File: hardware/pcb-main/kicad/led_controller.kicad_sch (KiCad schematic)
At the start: 5 parts, among them IC1 SN74AHCT125PWR

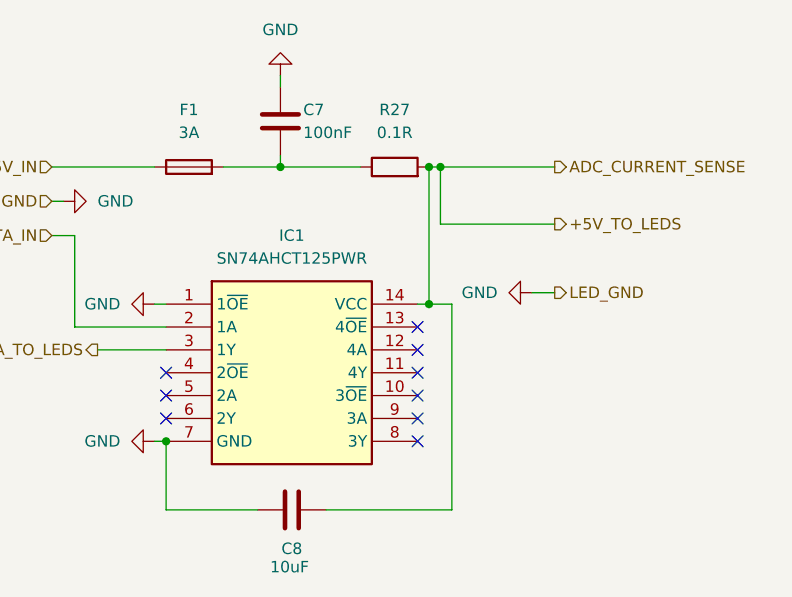
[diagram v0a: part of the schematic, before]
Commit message: Finished sensor redesign
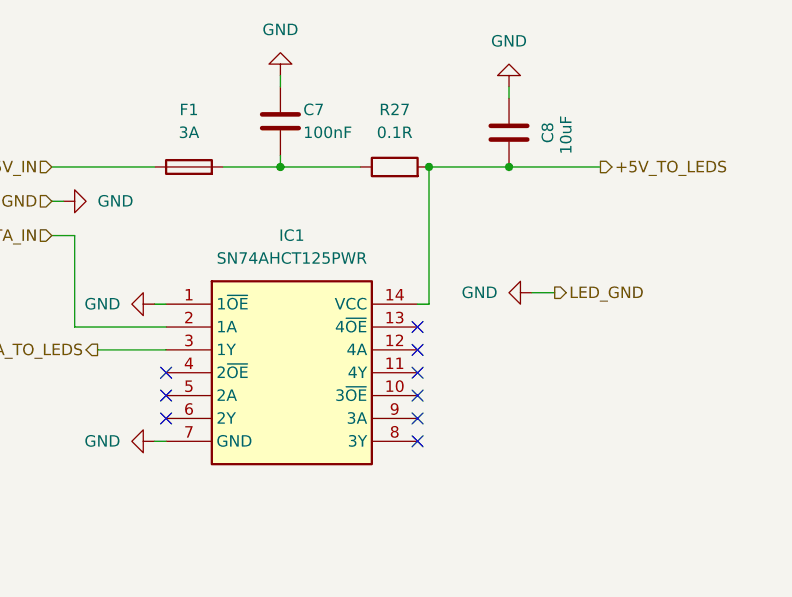
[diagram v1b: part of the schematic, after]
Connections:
- net +5V_TO_LEDS: now also C8.2; no longer C8.1
- net GND: now also C8.1; no longer C8.2
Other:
- moved on the sheet: C8
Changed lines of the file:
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@@
 	)
 	(junction
-		(at 146.05 88.9)
+		(at 184.15 58.42)
 		(diameter 0)
 		(color 0 0 0 0)
@@
 	)
 	(junction
-		(at 175.26 73.66)
-		(diameter 0)
-		(color 0 0 0 0)
-	)
-	(junction
-		(at 176.53 58.42)
-		(diameter 0)
-		(color 0 0 0 0)
-	)
-	(junction
 		(at 175.26 58.42)
 		(diameter 0)
@@
 	(wire
 		(pts
-			(xy 146.05 96.52) (xy 156.21 96.52)
-		)
-		(stroke
-			(width 0)
-			(type default)
-		)
-	)
-	(wire
-		(pts
-			(xy 176.53 64.77) (xy 176.53 58.42)
+			(xy 184.15 49.53) (xy 184.15 50.8)
 		)
 		(stroke
@@
 	(wire
 		(pts
-			(xy 176.53 58.42) (xy 189.23 58.42)
-		)
-		(stroke
-			(width 0)
-			(type default)
-		)
-	)
-	(wire
-		(pts
-			(xy 163.83 96.52) (xy 177.8 96.52)
-		)
-		(stroke
-			(width 0)
-			(type default)
-		)
-	)
-	(wire
-		(pts
 			(xy 144.78 88.9) (xy 146.05 88.9)
 		)
@@
 	(wire
 		(pts
-			(xy 177.8 73.66) (xy 175.26 73.66)
-		)
-		(stroke
-			(width 0)
-			(type default)
-		)
-	)
-	(wire
-		(pts
-			(xy 175.26 58.42) (xy 176.53 58.42)
+			(xy 184.15 58.42) (xy 194.31 58.42)
+		)
+		(stroke
+			(width 0)
+			(type default)
+		)
+	)
+	(wire
+		(pts
+			(xy 175.26 58.42) (xy 184.15 58.42)
 		)
 		(stroke
@@
 	(wire
 		(pts
-			(xy 189.23 64.77) (xy 176.53 64.77)
-		)
-		(stroke
-			(width 0)
-			(type default)
-		)
-	)
-	(wire
-		(pts
-			(xy 177.8 96.52) (xy 177.8 73.66)
-		)
-		(stroke
-			(width 0)
-			(type default)
-		)
-	)
-	(wire
-		(pts
 			(xy 152.4 58.42) (xy 158.75 58.42)
-		)
-		(stroke
-			(width 0)
-			(type default)
-		)
-	)
-	(wire
-		(pts
-			(xy 146.05 88.9) (xy 146.05 96.52)
 		)
 		(stroke
@@
 	(hierarchical_label "+5V_TO_LEDS"
 		(shape output)
-		(at 189.23 64.77 0)
-		(effects
-			(font
-				(size 1.27 1.27)
-			)
-			(justify left)
-		)
-	)
-	(hierarchical_label "ADC_CURRENT_SENSE"
-		(shape output)
-		(at 189.23 58.42 0)
+		(at 194.31 58.42 0)
 		(effects
 			(font
@@
 	(symbol
 		(lib_id "Device:C")
-		(at 160.02 96.52 270)
+		(at 184.15 54.61 0)
 		(unit 1)
 		(exclude_from_sim no)
@@
 		(dnp no)
 		(property "Reference" "C8"
-			(at 160.02 100.838 90)
+			(at 188.468 54.61 90)
 			(effects
 				(font
@@
 		)
 		(property "Value" "10uF"
-			(at 159.766 102.87 90)
+			(at 190.5 54.864 90)
 			(effects
 				(font
@@
 		)
 		(property "Footprint" "Capacitor_SMD:C_0603_1608Metric"
-			(at 156.21 97.4852 0)
+			(at 185.1152 58.42 0)
 			(effects
 				(font
@@
 		)
 		(property "Datasheet" "~"
-			(at 160.02 96.52 0)
+			(at 184.15 54.61 0)
 			(effects
 				(font
@@
 		)
 		(property "Description" "10uF capacitor"
-			(at 160.02 96.52 0)
+			(at 184.15 54.61 0)
 			(effects
 				(font
@@
 		)
 		(property "LCSC Part No" "C19702"
-			(at 160.02 96.52 0)
+			(at 184.15 54.61 0)
 			(effects
 				(font
@@
 		)
 		(property "LCSC Part" "C19702"
-			(at 160.02 96.52 90)
+			(at 184.15 54.61 90)
 			(effects
 				(font
@@
 					(unit 1)
 				)
+			)
+		)
+	)
+	(symbol
+		(lib_id "power:GND")
+		(at 184.15 49.53 180)
+		(unit 1)
+		(exclude_from_sim no)
+		(in_bom yes)
+		(on_board yes)
+		(dnp no)
+		(fields_autoplaced yes)
+		(property "Reference" "#PWR05"
+			(at 184.15 43.18 0)
+			(effects
+				(font
+					(size 1.27 1.27)
+				)
+				(hide yes)
+			)
+		)
+		(property "Value" "GND"
+			(at 184.15 44.45 0)
+			(effects
+				(font
+					(size 1.27 1.27)
+				)
+			)
+		)
+		(property "Footprint" ""
+			(at 184.15 49.53 0)
+			(effects
+				(font
+					(size 1.27 1.27)
+				)
+				(hide yes)
+			)
+		)
+		(property "Datasheet" ""
+			(at 184.15 49.53 0)
+			(effects
+				(font
+					(size 1.27 1.27)
+				)
+				(hide yes)
+			)
+		)
+		(property "Description" "Power symbol creates a global label with name \"GND\" , ground"
+			(at 184.15 49.53 0)
+			(effects
+				(font
+					(size 1.27 1.27)
+				)
+				(hide yes)
+			)
+		)
+		(pin "1"
+		)
+		(instances
+			(project "motion-play-main"
+				(path "/6e095bf3-d8d5-4f67-b79f-a2965409c7a9/22a71174-d1ab-41ca-9de7-73d077ebe0b0"
+					(reference "#PWR05")
+					(unit 1)
+				)

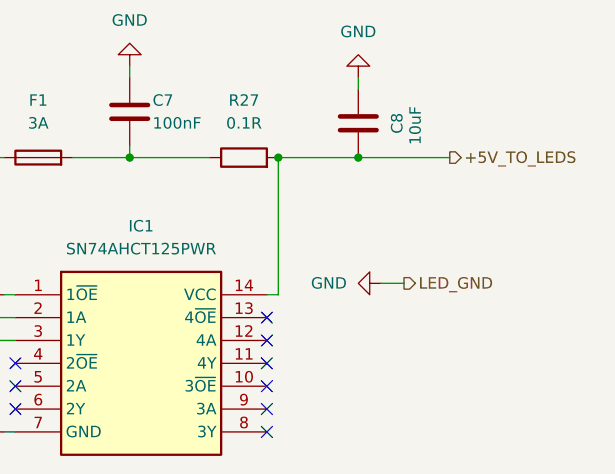
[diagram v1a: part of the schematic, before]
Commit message: Proximity detection and updated pcbs
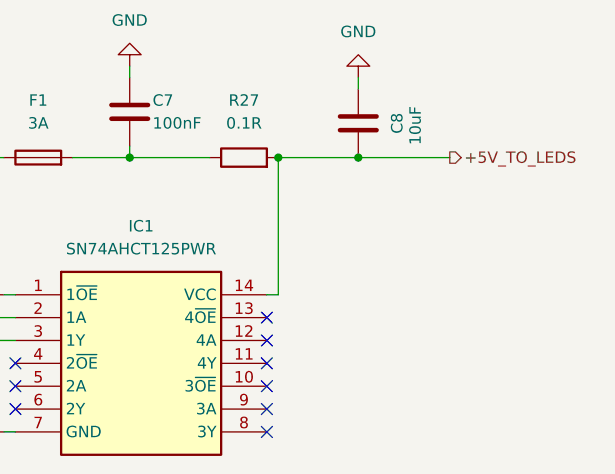
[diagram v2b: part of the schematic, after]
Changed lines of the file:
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@@
-	(wire
-		(pts
-			(xy 186.69 72.39) (xy 189.23 72.39)
-		)
-		(stroke
-			(width 0)
-			(type default)
-		)
-	)
 	(wire
 		(pts
@@
 		)
 	)
-	(hierarchical_label "LED_GND"
-		(shape output)
-		(at 189.23 72.39 0)
-		(effects
-			(font
-				(size 1.27 1.27)
-			)
-			(justify left)
-		)
-	)
 	(hierarchical_label "+5V_IN"
 		(shape input)
@@
 		)
 	)
-	(symbol
-		(lib_id "power:GND")
-		(at 186.69 72.39 270)
-		(unit 1)
-		(exclude_from_sim no)
-		(in_bom yes)
-		(on_board yes)
-		(dnp no)
-		(fields_autoplaced yes)
-		(property "Reference" "#PWR021"
-			(at 180.34 72.39 0)
-			(effects
-				(font
-					(size 1.27 1.27)
-				)
-				(hide yes)
-			)
-		)
-		(property "Value" "GND"
-			(at 182.88 72.3899 90)
-			(effects
-				(font
-					(size 1.27 1.27)
-				)
-				(justify right)
-			)
-		)
-		(property "Footprint" ""
-			(at 186.69 72.39 0)
-			(effects
-				(font
-					(size 1.27 1.27)
-				)
-				(hide yes)
-			)
-		)
-		(property "Datasheet" ""
-			(at 186.69 72.39 0)
-			(effects
-				(font
-					(size 1.27 1.27)
-				)
-				(hide yes)
-			)
-		)
-		(property "Description" "Power symbol creates a global label with name \"GND\" , ground"
-			(at 186.69 72.39 0)
-			(effects
-				(font
-					(size 1.27 1.27)
-				)
-				(hide yes)
-			)
-		)
-		(pin "1"
-		)
-		(instances
-			(project "motion-play-main"
-				(path "/6e095bf3-d8d5-4f67-b79f-a2965409c7a9/22a71174-d1ab-41ca-9de7-73d077ebe0b0"
-					(reference "#PWR021")
-					(unit 1)
-				)
-			)
-		)
-	)

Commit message: Complete Phase 3b: annotate LED controller block, nets, and functional blocks
- Annotated final 6 components (IC1 level shifter, F1 fuse, R27 sense
  resistor, C7/C8 caps, J3 LED connector) → 37/37 components (100%)
- Added net annotations for all 26 nets (type, protocol, direction, description)
- Defined 5 functional blocks: power, mcu, i2c_mux, sensor_connectors,
  led_controller — with descriptions, component membership, and design notes
- Added top-level description and sheet_interface descriptions
- Re-extracted with --previous merge; KiCad round-trip save applied to all sheets

Made-with: Cursor
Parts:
- C7: ai_block (none) -> led_controller; ai_critical_specs (none) -> 100nF, 0603; ai_function (none) -> High-frequency bypass capacitor on intermediate LED power n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; ai_role (none) -> decoupling
- C8: ai_block (none) -> led_controller; ai_critical_specs (none) -> 10uF, 0603, placed near IC1 VCC and LED strip connector; ai_function (none) -> Bulk decoupling capacitor on +5V_TO_LEDS rail, stabilizes L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; ai_role (none) -> decoupling
- F1: ai_block (none) -> led_controller; ai_critical_specs (none) -> 3A rated, 1206 package, protects against LED strip short ci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; ai_function (none) -> Overcurrent protection fuse on +5V LED strip power path; ai_role (none) -> protection
- IC1: ai_block (none) -> led_controller; ai_critical_specs (none) -> AHCT family (3.3V input compatible with 5V VCC), only 1 of 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; ai_function (none) -> Quad bus buffer/level shifter, shifts LED data signal from 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; ai_role (none) -> level_shifter
- R27: ai_block (none) -> led_controller; ai_critical_specs (none) -> 0.1 ohm, 2512 package (high power), 1A = 0.1V drop; ai_function (none) -> Current sense resistor in LED strip +5V power path, enables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; ai_role (none) -> current_sense
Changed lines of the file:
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@@
 					(size 1.27 1.27)
 				)
-				(hide yes)
 			)
 		)
@@
 					(size 1.27 1.27)
 				)
-				(hide yes)
 			)
 		)
@@
 					(size 1.27 1.27)
 				)
-				(hide yes)
 			)
 		)
@@
 					(size 1.27 1.27)
 				)
-				(hide yes)
 			)
 		)
 		(property "LCSC Part" "C354897"
 			(at 148.59 58.42 90)
+			(effects
+				(font
+					(size 1.27 1.27)
+				)
+			)
+		)
+		(property "ai_block" "led_controller"
+			(at 0 0 0)
+			(effects
+				(font
+					(size 1.27 1.27)
+				)
+				(hide yes)
+			)
+		)
+		(property "ai_critical_specs" "3A rated, 1206 package, protects against LED strip short circuit"
+			(at 0 0 0)
+			(effects
+				(font
+					(size 1.27 1.27)
+				)
+				(hide yes)
+			)
+		)
+		(property "ai_function" "Overcurrent protection fuse on +5V LED strip power path"
+			(at 0 0 0)
+			(effects
+				(font
+					(size 1.27 1.27)
+				)
+				(hide yes)
+			)
+		)
+		(property "ai_role" "protection"
+			(at 0 0 0)
 			(effects
 				(font
@@
 					(size 1.27 1.27)
 				)
-				(hide yes)
 			)
 		)
@@
 					(size 1.27 1.27)
 				)
-				(hide yes)
 			)
 		)
@@
 					(size 1.27 1.27)
 				)
-				(hide yes)
 			)
 		)
@@
 					(size 1.27 1.27)
 				)
-				(hide yes)
 			)
 		)
 		(property "LCSC Part" "C500724"
 			(at 171.45 58.42 90)
+			(effects
+				(font
+					(size 1.27 1.27)
+				)
+			)
+		)
+		(property "ai_block" "led_controller"
+			(at 0 0 0)
+			(effects
+				(font
+					(size 1.27 1.27)
+				)
+				(hide yes)
+			)
+		)
+		(property "ai_critical_specs" "0.1 ohm, 2512 package (high power), 1A = 0.1V drop"
+			(at 0 0 0)
+			(effects
+				(font
+					(size 1.27 1.27)
+				)
+				(hide yes)
+			)
+		)
+		(property "ai_function" "Current sense resistor in LED strip +5V power path, enables measuring LED strip current draw"
+			(at 0 0 0)
+			(effects
+				(font
+					(size 1.27 1.27)
+				)
+				(hide yes)
+			)
+		)
+		(property "ai_role" "current_sense"
+			(at 0 0 0)
 			(effects
 				(font
@@
 					(size 1.27 1.27)
 				)
-				(hide yes)
 			)
 		)
@@
 					(size 1.27 1.27)
 				)
-				(hide yes)
 			)
 		)
@@
 					(size 1.27 1.27)
 				)
-				(hide yes)
 			)
 		)
@@
 					(size 1.27 1.27)
 				)
-				(hide yes)
 			)
 		)
@@
 					(size 1.27 1.27)
 				)
-				(hide yes)
 			)
 		)
@@
 					(size 1.27 1.27)
 				)
-				(hide yes)
 			)
 		)
@@
 					(size 1.27 1.27)
 				)
-				(hide yes)
 			)
 		)
@@
 					(size 1.27 1.27)
 				)
-				(hide yes)
 			)
 		)
 		(property "LCSC Part" "C19702"
 			(at 184.15 54.61 90)
+			(effects
+				(font
+					(size 1.27 1.27)
+				)
+			)
+		)
+		(property "ai_block" "led_controller"
+			(at 0 0 0)
+			(effects
+				(font
+					(size 1.27 1.27)
+				)
+				(hide yes)
+			)
+		)
+		(property "ai_critical_specs" "10uF, 0603, placed near IC1 VCC and LED strip connector"
+			(at 0 0 0)
+			(effects
+				(font
+					(size 1.27 1.27)
+				)
+				(hide yes)
+			)
+		)
+		(property "ai_function" "Bulk decoupling capacitor on +5V_TO_LEDS rail, stabilizes LED strip power"
+			(at 0 0 0)
+			(effects
+				(font
+					(size 1.27 1.27)
+				)
+				(hide yes)
+			)
+		)
+		(property "ai_role" "decoupling"
+			(at 0 0 0)
 			(effects
 				(font
@@
 					(size 1.27 1.27)
 				)
-				(hide yes)
 			)
 		)
@@
 					(size 1.27 1.27)
 				)
-				(hide yes)
 			)
 		)
@@
 					(size 1.27 1.27)
 				)
-				(hide yes)
 			)
 		)
@@
 					(size 1.27 1.27)
 				)
-				(hide yes)
 			)
 		)
@@
 				)
 				(justify left top)
-				(hide yes)
 			)
 		)
@@
 				)
 				(justify left top)
-				(hide yes)
 			)
 		)
@@
 					(size 1.27 1.27)
 				)
-				(hide yes)
 			)
 		)
@@
 				)
 				(justify left top)
-				(hide yes)
 			)
 		)
@@
 				)
 				(justify left top)
-				(hide yes)
 			)
 		)
@@
 				)
 				(justify left top)
-				(hide yes)
 			)
 		)
@@
 				)
 				(justify left top)
-				(hide yes)
 			)
 		)
@@
 				)
 				(justify left top)
-				(hide yes)
 			)
 		)
 		(property "LCSC Part" "C36365"
 			(at 146.05 73.66 0)
+			(effects
+				(font
+					(size 1.27 1.27)
+				)
+			)
+		)
+		(property "ai_block" "led_controller"
+			(at 0 0 0)
+			(effects
+				(font
+					(size 1.27 1.27)
+				)
+				(hide yes)
+			)
+		)
+		(property "ai_critical_specs" "AHCT family (3.3V input compatible with 5V VCC), only 1 of 4 buffers used (1A->1Y)"
+			(at 0 0 0)
+			(effects
+				(font
+					(size 1.27 1.27)
+				)
+				(hide yes)
+			)
+		)
+		(property "ai_function" "Quad bus buffer/level shifter, shifts LED data signal from 3.3V MCU logic to 5V WS2812B logic"
+			(at 0 0 0)
+			(effects
+				(font
+					(size 1.27 1.27)
+				)
+				(hide yes)
+			)
+		)
+		(property "ai_role" "level_shifter"
+			(at 0 0 0)
 			(effects
 				(font
@@
 					(size 1.27 1.27)
 				)
-				(hide yes)
 			)
 		)
@@
 					(size 1.27 1.27)
 				)
-				(hide yes)
 			)
 		)
@@
 					(size 1.27 1.27)
 				)
-				(hide yes)
 			)
 		)
@@
 					(size 1.27 1.27)
 				)
-				(hide yes)
 			)
 		)
@@
 		(on_board yes)
 		(dnp no)
-		(fields_autoplaced yes)
 		(property "Reference" "#PWR019"
 			(at 140.97 62.23 0)
@@
 					(size 1.27 1.27)
 				)
-				(hide yes)
 			)
 		)
@@
 					(size 1.27 1.27)
 				)
-				(hide yes)
 			)
 		)
@@
 					(size 1.27 1.27)
 				)
-				(hide yes)
 			)
 		)
 		(property "Description" "Power symbol creates a global label with name \"GND\" , ground"
-			(at 134.62 62.23 0)
-			(effects
-				(font
-					(size 1.27 1.27)
-				)
-				(hide yes)
+			(at 135.89 61.976 0)
+			(effects
+				(font
+					(size 1.27 1.27)
+				)
 			)
 		)
@@
 					(size 1.27 1.27)
 				)
-				(hide yes)
 			)
 		)
@@
 					(size 1.27 1.27)
 				)
-				(hide yes)
 			)
 		)
@@
 					(size 1.27 1.27)
 				)
-				(hide yes)
 			)
 		)
@@
 					(size 1.27 1.27)
 				)
-				(hide yes)
 			)
 		)
 		(property "LCSC Part" "C14663"
 			(at 158.75 53.34 0)
+			(effects
+				(font
+					(size 1.27 1.27)
+				)
+			)
+		)
+		(property "ai_block" "led_controller"
+			(at 0 0 0)
+			(effects
+				(font
+					(size 1.27 1.27)
+				)
+				(hide yes)
+			)
+		)
+		(property "ai_critical_specs" "100nF, 0603"
+			(at 0 0 0)
+			(effects
+				(font
+					(size 1.27 1.27)
+				)
+				(hide yes)
+			)
+		)
+		(property "ai_function" "High-frequency bypass capacitor on intermediate LED power node (between fuse F1 and sense resistor R27)"
+			(at 0 0 0)
+			(effects
+				(font
+					(size 1.27 1.27)
+				)
+				(hide yes)
+			)
+		)
+		(property "ai_role" "decoupling"
+			(at 0 0 0)
 			(effects
 				(font
@@
 					(size 1.27 1.27)
 				)
-				(hide yes)
 			)
 		)
@@
 					(size 1.27 1.27)
 				)
-				(hide yes)
 			)
 		)
@@
 					(size 1.27 1.27)
 				)
-				(hide yes)
 			)
 		)
@@
 					(size 1.27 1.27)
 				)
-				(hide yes)
-			)
-		)
+			)
+		)

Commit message: Integrate power management sub-sheet into root schematic (Phase 3.6)
- Delete J2 (DWEII USB-C module) and D1 (Schottky) from root sheet
- Add hierarchical sheet reference to power_management.kicad_sch
- Wire 6 sheet pins: +5V, GND, +3.3V, I2C_SDA, I2C_SCL, CHRG_INT
- Connect CHRG_INT to GPIO 21 (U2 pin 19)
- Hide non-essential property labels (Description, Datasheet, etc.)
  across all original schematic sheets — only Reference and Value visible
- ERC: 0 errors on root/LED/TCA9548A sheets, 4 expected power_pin
  warnings on power management sheet (net labels vs PWR_FLAG)

Made-with: Cursor
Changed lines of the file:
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@@
 					(size 1.27 1.27)
 				)
+				(hide yes)
 			)
 		)
@@
 					(size 1.27 1.27)
 				)
+				(hide yes)
 			)
 		)
@@
 					(size 1.27 1.27)
 				)
+				(hide yes)
 			)
 		)
@@
 					(size 1.27 1.27)
 				)
+				(hide yes)
 			)
 		)
@@
 					(size 1.27 1.27)
 				)
+				(hide yes)
 			)
 		)
@@
 					(size 1.27 1.27)
 				)
+				(hide yes)
 			)
 		)
@@
 					(size 1.27 1.27)
 				)
+				(hide yes)
 			)
 		)
@@
 					(size 1.27 1.27)
 				)
+				(hide yes)
 			)
 		)
@@
 					(size 1.27 1.27)
 				)
+				(hide yes)
 			)
 		)
@@
 					(size 1.27 1.27)
 				)
+				(hide yes)
 			)
 		)
@@
 					(size 1.27 1.27)
 				)
+				(hide yes)
 			)
 		)
@@
 					(size 1.27 1.27)
 				)
+				(hide yes)
 			)
 		)
@@
 					(size 1.27 1.27)
 				)
+				(hide yes)
 			)
 		)
@@
 					(size 1.27 1.27)
 				)
+				(hide yes)
 			)
 		)
@@
 					(size 1.27 1.27)
 				)
+				(hide yes)
 			)
 		)
@@
 					(size 1.27 1.27)
 				)
+				(hide yes)
 			)
 		)
@@
 					(size 1.27 1.27)
 				)
+				(hide yes)
 			)
 		)
@@
 					(size 1.27 1.27)
 				)
+				(hide yes)
 			)
 		)
@@
 					(size 1.27 1.27)
 				)
+				(hide yes)
 			)
 		)
@@
 					(size 1.27 1.27)
 				)
+				(hide yes)
 			)
 		)
@@
 					(size 1.27 1.27)
 				)
+				(hide yes)
 			)
 		)
@@
 				)
 				(justify left top)
+				(hide yes)
 			)
 		)
@@
 				)
 				(justify left top)
+				(hide yes)
 			)
 		)
@@
 					(size 1.27 1.27)
 				)
+				(hide yes)
 			)
 		)
@@
 				)
 				(justify left top)
+				(hide yes)
 			)
 		)
@@
 				)
 				(justify left top)
+				(hide yes)
 			)
 		)
@@
 				)
 				(justify left top)
+				(hide yes)
 			)
 		)
@@
 				)
 				(justify left top)
+				(hide yes)
 			)
 		)
@@
 				)
 				(justify left top)
+				(hide yes)
 			)
 		)
@@
 					(size 1.27 1.27)
 				)
+				(hide yes)
 			)
 		)
@@
 					(size 1.27 1.27)
 				)
+				(hide yes)
 			)
 		)
@@
 					(size 1.27 1.27)
 				)
+				(hide yes)
 			)
 		)
@@
 					(size 1.27 1.27)
 				)
+				(hide yes)
 			)
 		)
@@
 					(size 1.27 1.27)
 				)
+				(hide yes)
 			)
 		)
@@
 					(size 1.27 1.27)
 				)
+				(hide yes)
 			)
 		)
@@
 					(size 1.27 1.27)
 				)
+				(hide yes)
 			)
 		)
@@
 					(size 1.27 1.27)
 				)
+				(hide yes)
 			)
 		)
@@
 					(size 1.27 1.27)
 				)
+				(hide yes)
 			)
 		)
@@
 					(size 1.27 1.27)
 				)
+				(hide yes)
 			)
 		)
@@
 					(size 1.27 1.27)
 				)
+				(hide yes)
 			)
 		)
@@
 					(size 1.27 1.27)
 				)
+				(hide yes)
 			)
 		)
@@
 					(size 1.27 1.27)
 				)
+				(hide yes)
 			)
 		)
@@
 					(size 1.27 1.27)
 				)
+				(hide yes)
 			)
 		)
@@
 					(size 1.27 1.27)
 				)
-			)
-		)
+				(hide yes)
+			)
+		)

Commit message: JLCPCB pre-flight review: fix 3 LCSC part numbers, add fabrication files
Pre-flight review for JLCPCB fabrication + SMT assembly submission.

LCSC part fixes (data-only, no schematic/PCB design changes):
- J4/J5/J6: C160403 (3-pin JST-SH) → C136657 (5-pin SM05B-SRSS-TB)
- R27: C500724 (0.1Ω 2W, out of stock) → C2903476 (0.1Ω 3W, 94k stock)
- Q2: C3040193 (VBZ3401, 3 units) → C15127 (AO3401A, 1.45M stock, Basic)

Adds fabrication exports (Fabrication Toolkit plugin):
- BOM, CPL/positions, designators, netlist
- DRC and ERC reports
- Pre-flight review report (preflight-review.md)

Remaining advisory: BQ24195RGER (C90862) has only 22 units — order soon.

Made-with: Cursor
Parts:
- R27: LCSC Part C500724 -> C2903476; LCSC Part No C500724 -> C2903476
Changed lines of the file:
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@@
 			)
 		)
-		(property "LCSC Part No" "C500724"
+		(property "LCSC Part No" "C2903476"
 			(at 171.45 58.42 0)
 			(effects
@@
 			)
 		)
-		(property "LCSC Part" "C500724"
+		(property "LCSC Part" "C2903476"
 			(at 171.45 58.42 90)
 			(effects
